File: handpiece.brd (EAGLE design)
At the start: 100 x 82.5 mm, 27 parts, among them IC1 MEGA8-P

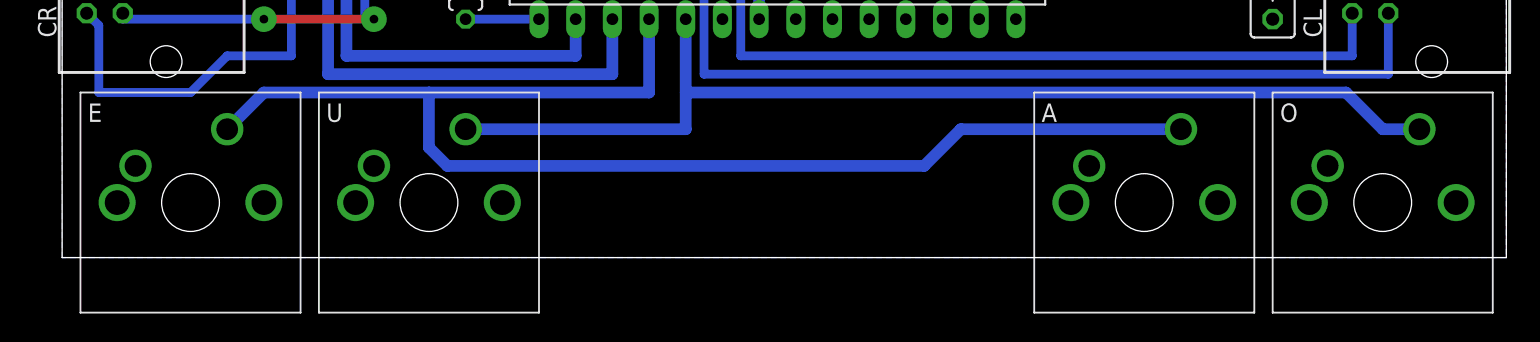
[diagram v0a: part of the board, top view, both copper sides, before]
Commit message: move vocal keys to comply to https://sites.google.com/site/ploverdoc/lesson-1-fingers-and-keys
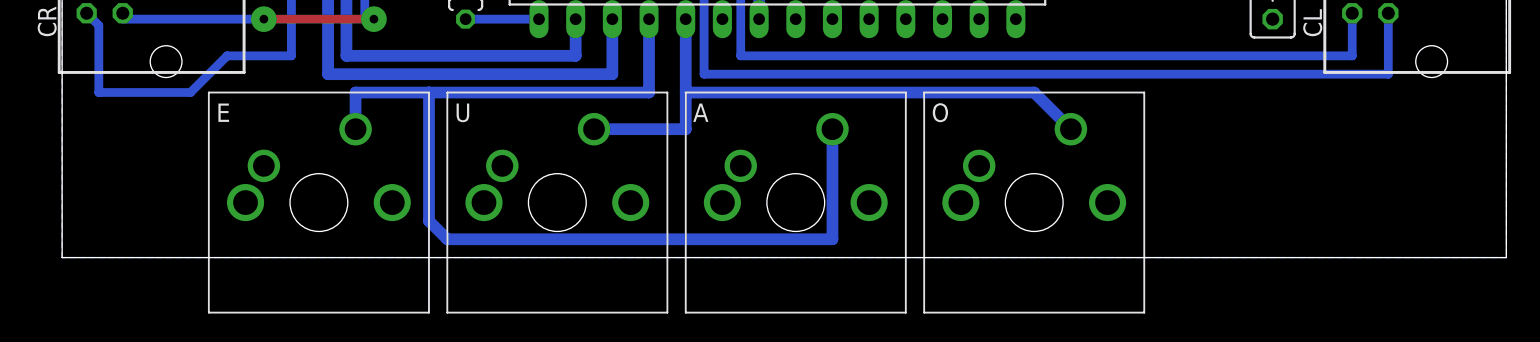
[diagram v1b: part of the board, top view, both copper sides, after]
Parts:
- moved A 24.1 mm to (50.8, 2.54)
- moved O 24.1 mm to (67.3, 2.54)
- moved E 8.89 mm to (17.8, 2.54)
- moved U 8.89 mm to (34.3, 2.54)
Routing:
- net OU: track 74.7 -> 41.7 mm
- net EA: track 92.8 -> 72.9 mm
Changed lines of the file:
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@@
 <?xml version="1.0" encoding="utf-8"?>
 <!DOCTYPE eagle SYSTEM "eagle.dtd">
-<eagle version="6.5.0">
+<eagle version="6.4">
 <drawing>
 <settings>
@@
 <element name="D" library="cherrymx" package="CHERRY-MX-I" value="CHERRY-MX-I" x="91.44" y="52.07"/>
 <element name="Z" library="cherrymx" package="CHERRY-MX-I" value="CHERRY-MX-I" x="91.44" y="35.56"/>
-<element name="E" library="cherrymx" package="CHERRY-MX-I" value="CHERRY-MX-I" x="8.89" y="2.54"/>
-<element name="U" library="cherrymx" package="CHERRY-MX-I" value="CHERRY-MX-I" x="25.4" y="2.54"/>
-<element name="O" library="cherrymx" package="CHERRY-MX-I" value="CHERRY-MX-I" x="91.44" y="2.54"/>
-<element name="A" library="cherrymx" package="CHERRY-MX-I" value="CHERRY-MX-I" x="74.93" y="2.54"/>
+<element name="E" library="cherrymx" package="CHERRY-MX-I" value="CHERRY-MX-I" x="17.78" y="2.54"/>
+<element name="U" library="cherrymx" package="CHERRY-MX-I" value="CHERRY-MX-I" x="34.29" y="2.54"/>
+<element name="O" library="cherrymx" package="CHERRY-MX-I" value="CHERRY-MX-I" x="67.31" y="2.54"/>
+<element name="A" library="cherrymx" package="CHERRY-MX-I" value="CHERRY-MX-I" x="50.8" y="2.54"/>
 <element name="SS0" library="cherrymx" package="CHERRY-MX-I" value="CHERRY-MX-I" x="8.89" y="52.07"/>
 <element name="IC1" library="atmel" package="DIL28-3" value="MEGA8-P" x="49.53" y="19.05">
@@
 <contactref element="CR" pad="2"/>
 <wire x1="50.8" y1="15.24" x2="50.8" y2="22.86" width="0" layer="19" extent="1-1"/>
+<wire x1="46.99" y1="5.08" x2="50.8" y2="15.24" width="0" layer="19" extent="1-1"/>
 <wire x1="71.12" y1="38.1" x2="54.61" y2="38.1" width="0" layer="19" extent="1-1"/>
 </signal>
@@
 <signal name="EA">
 <contactref element="E" pad="PIN-2"/>
-<wire x1="11.43" y1="7.62" x2="13.97" y2="10.16" width="0.8128" layer="16"/>
-<wire x1="13.97" y1="10.16" x2="25.4" y2="10.16" width="0.8128" layer="16"/>
+<wire x1="20.32" y1="7.62" x2="20.32" y2="10.16" width="0.8128" layer="16"/>
+<wire x1="20.32" y1="10.16" x2="25.4" y2="10.16" width="0.8128" layer="16"/>
 <wire x1="25.4" y1="10.16" x2="40.64" y2="10.16" width="0.8128" layer="16"/>
 <contactref element="A" pad="PIN-2"/>
-<wire x1="25.4" y1="10.16" x2="25.4" y2="6.35" width="0.8128" layer="16"/>
-<wire x1="25.4" y1="6.35" x2="26.67" y2="5.08" width="0.8128" layer="16"/>
-<wire x1="26.67" y1="5.08" x2="59.69" y2="5.08" width="0.8128" layer="16"/>
-<wire x1="59.69" y1="5.08" x2="62.23" y2="7.62" width="0.8128" layer="16"/>
-<wire x1="62.23" y1="7.62" x2="77.47" y2="7.62" width="0.8128" layer="16"/>
+<wire x1="25.4" y1="10.16" x2="25.4" y2="1.27" width="0.8128" layer="16"/>
+<wire x1="25.4" y1="1.27" x2="26.67" y2="0" width="0.8128" layer="16"/>
+<wire x1="26.67" y1="0" x2="53.34" y2="0" width="0.8128" layer="16"/>
+<wire x1="53.34" y1="0" x2="53.34" y2="7.62" width="0.8128" layer="16"/>
 <contactref element="IC1" pad="4"/>
 <wire x1="40.64" y1="10.16" x2="40.64" y2="15.24" width="0.8128" layer="16"/>
@@
 <signal name="OU">
 <contactref element="U" pad="PIN-2"/>
-<wire x1="27.94" y1="7.62" x2="43.18" y2="7.62" width="0.8128" layer="16"/>
+<wire x1="36.83" y1="7.62" x2="43.18" y2="7.62" width="0.8128" layer="16"/>
 <contactref element="O" pad="PIN-2"/>
 <wire x1="43.18" y1="7.62" x2="43.18" y2="10.16" width="0.8128" layer="16"/>
-<wire x1="43.18" y1="10.16" x2="88.9" y2="10.16" width="0.8128" layer="16"/>
-<wire x1="88.9" y1="10.16" x2="91.44" y2="7.62" width="0.8128" layer="16"/>
-<wire x1="91.44" y1="7.62" x2="93.98" y2="7.62" width="0.8128" layer="16"/>
+<wire x1="43.18" y1="10.16" x2="67.31" y2="10.16" width="0.8128" layer="16"/>
+<wire x1="67.31" y1="10.16" x2="69.85" y2="7.62" width="0.8128" layer="16"/>
 <contactref element="IC1" pad="5"/>
 <wire x1="43.18" y1="15.24" x2="43.18" y2="10.16" width="0.8128" layer="16"/>

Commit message: exchange minidin connectors with raw soldering pads and strain-releive holes
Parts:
- removed CL, CR: (no value), con-yamaichi:MDIN06SS
- added JPL, JPR: (no value), pinhead:1X04
- moved C1 7.62 mm to (83.8, 11.4)
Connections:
- net GND: now also JPL.1, JPR.1; no longer CL.1, CL.2, CR.1, CR.2
- net SCL: now also JPL.4, JPR.4; no longer CL.6, CR.6
- net SDA: now also JPL.3, JPR.3; no longer CL.4, CR.4
- net VCC: now also JPL.2, JPR.2; no longer CL.3, CL.5, CR.3, CR.5
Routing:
- net SCL: track 130.1 -> 113.4 mm
- net VCC: track 108.5 -> 124.5 mm
- net SDA: track 130.1 -> 138.2 mm
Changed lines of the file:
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@@
 <layer number="43" name="vRestrict" color="2" fill="10" visible="yes" active="yes"/>
 <layer number="44" name="Drills" color="7" fill="1" visible="no" active="yes"/>
-<layer number="45" name="Holes" color="7" fill="1" visible="no" active="yes"/>
+<layer number="45" name="Holes" color="7" fill="1" visible="yes" active="yes"/>
 <layer number="46" name="Milling" color="3" fill="1" visible="no" active="yes"/>
 <layer number="47" name="Measures" color="7" fill="1" visible="no" active="yes"/>
@@
 <wire x1="100" y1="81.27" x2="0" y2="81.27" width="0" layer="20"/>
 <wire x1="0" y1="81.27" x2="0" y2="-1.27" width="0" layer="20"/>
+<hole x="3.81" y="16.51" drill="2.2"/>
+<hole x="3.81" y="10.16" drill="2.2"/>
+<hole x="95.25" y="16.51" drill="2.2"/>
+<hole x="95.25" y="10.16" drill="2.2"/>
 </plain>
 <attributes>
@@
 </element>
 <element name="R1" library="rcl" package="0207/7" value="10k" x="27.94" y="19.05" rot="R90"/>
-<element name="C1" library="rcl" package="C075-032X103" value="100n" x="83.82" y="19.05" rot="R270"/>
-<element name="CL" library="con-yamaichi" package="MDIN06SS" value="" x="100.33" y="19.05" rot="R90">
-<attribute name="OC_NEWARK" value="unknown" x="100.33" y="19.05" size="1.778" layer="27" rot="R90" display="off"/>
-<attribute name="MPN" value="" x="100.33" y="19.05" size="1.778" layer="27" rot="R90" display="off"/>
-<attribute name="MF" value="" x="100.33" y="19.05" size="1.778" layer="27" rot="R90" display="off"/>
-<attribute name="OC_FARNELL" value="unknown" x="100.33" y="19.05" size="1.778" layer="27" rot="R90" display="off"/>
-</element>
-<element name="CR" library="con-yamaichi" package="MDIN06SS" value="" x="12.7" y="19.05" rot="R90">
-<attribute name="OC_NEWARK" value="unknown" x="12.7" y="19.05" size="1.778" layer="27" rot="R90" display="off"/>
-<attribute name="MPN" value="" x="12.7" y="19.05" size="1.778" layer="27" rot="R90" display="off"/>
-<attribute name="MF" value="" x="12.7" y="19.05" size="1.778" layer="27" rot="R90" display="off"/>
-<attribute name="OC_FARNELL" value="unknown" x="12.7" y="19.05" size="1.778" layer="27" rot="R90" display="off"/>
-</element>
+<element name="C1" library="rcl" package="C075-032X103" value="100n" x="83.82" y="11.43" rot="R270"/>
+<element name="JPL" library="pinhead" package="1X04" value="" x="7.62" y="22.86"/>
+<element name="JPR" library="pinhead" package="1X04" value="" x="91.44" y="22.86" rot="R180"/>
 </elements>
 <signals>
@@
 <contactref element="D" pad="PIN-1"/>
 <contactref element="Z" pad="PIN-1"/>
-<contactref element="CL" pad="1"/>
-<contactref element="CL" pad="2"/>
 <contactref element="E" pad="PIN-1"/>
 <contactref element="U" pad="PIN-1"/>
@@
 <vertex x="0" y="-1.27"/>
 </polygon>
-<contactref element="CR" pad="1"/>
-<contactref element="CR" pad="2"/>
-<wire x1="50.8" y1="15.24" x2="50.8" y2="22.86" width="0" layer="19" extent="1-1"/>
+<contactref element="JPL" pad="1"/>
+<contactref element="JPR" pad="1"/>
+<wire x1="50.8" y1="22.86" x2="50.8" y2="15.24" width="0" layer="19" extent="1-1"/>
 <wire x1="46.99" y1="5.08" x2="50.8" y2="15.24" width="0" layer="19" extent="1-1"/>
 <wire x1="71.12" y1="38.1" x2="54.61" y2="38.1" width="0" layer="19" extent="1-1"/>
@@
 <contactref element="R1" pad="2"/>
 <contactref element="C1" pad="1"/>
-<contactref element="CL" pad="3"/>
-<contactref element="CL" pad="5"/>
 <wire x1="27.94" y1="22.86" x2="27.94" y2="20.32" width="0.8128" layer="16"/>
 <wire x1="27.94" y1="20.32" x2="48.26" y2="20.32" width="0.8128" layer="16"/>
@@
 <wire x1="53.34" y1="22.86" x2="53.34" y2="20.32" width="0.8128" layer="16"/>
 <wire x1="53.34" y1="17.78" x2="83.82" y2="17.78" width="0.8128" layer="16"/>
-<wire x1="83.82" y1="17.78" x2="83.82" y2="22.86" width="0.8128" layer="16"/>
-<wire x1="83.82" y1="22.86" x2="88.92" y2="22.86" width="0.8128" layer="16"/>
-<wire x1="91.83" y1="22.45" x2="89.33" y2="22.45" width="0.8128" layer="16"/>
-<wire x1="89.33" y1="22.45" x2="88.92" y2="22.86" width="0.8128" layer="16"/>
-<contactref element="CR" pad="3"/>
-<contactref element="CR" pad="5"/>
-<wire x1="1.7" y1="22.45" x2="4.2" y2="22.45" width="0.8128" layer="16"/>
-<wire x1="4.2" y1="22.45" x2="13.97" y2="22.45" width="0.8128" layer="16"/>
-<wire x1="13.97" y1="22.45" x2="13.97" y2="22.86" width="0.8128" layer="16"/>
-<via x="13.97" y="22.86" extent="1-16" drill="0.6" diameter="1.778" shape="square"/>
-<wire x1="13.97" y1="22.86" x2="25.4" y2="22.86" width="0.8128" layer="1"/>
+<wire x1="83.82" y1="17.78" x2="83.82" y2="15.24" width="0.8128" layer="16"/>
+<via x="15.24" y="22.86" extent="1-16" drill="0.6" diameter="1.778" shape="square"/>
+<wire x1="15.24" y1="22.86" x2="25.4" y2="22.86" width="0.8128" layer="1"/>
 <via x="25.4" y="22.86" extent="1-16" drill="0.6" diameter="1.778" shape="square"/>
 <wire x1="53.34" y1="17.78" x2="53.34" y2="20.32" width="0.8128" layer="16"/>
 <wire x1="53.34" y1="20.32" x2="48.26" y2="20.32" width="0.8128" layer="16"/>
 <wire x1="25.4" y1="22.86" x2="27.94" y2="22.86" width="0.8128" layer="16"/>
+<contactref element="JPL" pad="2"/>
+<contactref element="JPR" pad="2"/>
+<wire x1="15.24" y1="22.86" x2="15.24" y2="25.4" width="0.6096" layer="16"/>
+<wire x1="15.24" y1="25.4" x2="6.35" y2="25.4" width="0.6096" layer="16"/>
+<wire x1="6.35" y1="25.4" x2="6.35" y2="22.86" width="0.6096" layer="16"/>
+<wire x1="83.82" y1="15.24" x2="83.82" y2="27.94" width="0.8128" layer="16"/>
+<wire x1="83.82" y1="27.94" x2="92.71" y2="27.94" width="0.8128" layer="16"/>
+<wire x1="92.71" y1="27.94" x2="92.71" y2="22.86" width="0.8128" layer="16"/>
 </signal>
 <signal name="N$2">
@@
 <signal name="SCL">
 <contactref element="IC1" pad="28"/>
-<contactref element="CL" pad="6"/>
-<contactref element="CR" pad="6"/>
-<wire x1="89.33" y1="15.65" x2="89.33" y2="12.7" width="0.6096" layer="16"/>
-<wire x1="89.33" y1="12.7" x2="46.99" y2="12.7" width="0.6096" layer="16"/>
+<wire x1="87.63" y1="12.7" x2="46.99" y2="12.7" width="0.6096" layer="16"/>
 <wire x1="46.99" y1="12.7" x2="46.99" y2="19.05" width="0.6096" layer="16"/>
 <wire x1="46.99" y1="19.05" x2="23.495" y2="19.05" width="0.6096" layer="16"/>
@@
 <wire x1="27.94" y1="25.4" x2="30.48" y2="22.86" width="0.6096" layer="16"/>
 <wire x1="30.48" y1="22.86" x2="33.02" y2="22.86" width="0.6096" layer="16"/>
-<wire x1="23.495" y1="19.05" x2="13.97" y2="19.05" width="0.6096" layer="1"/>
-<wire x1="13.97" y1="19.05" x2="15.875" y2="19.05" width="0.6096" layer="16"/>
-<wire x1="15.875" y1="19.05" x2="15.875" y2="12.7" width="0.6096" layer="16"/>
-<wire x1="15.875" y1="12.7" x2="11.43" y2="12.7" width="0.6096" layer="16"/>
-<wire x1="11.43" y1="12.7" x2="8.89" y2="10.16" width="0.6096" layer="16"/>
-<wire x1="8.89" y1="10.16" x2="2.54" y2="10.16" width="0.6096" layer="16"/>
-<wire x1="2.54" y1="10.16" x2="2.54" y2="14.81" width="0.6096" layer="16"/>
-<wire x1="2.54" y1="14.81" x2="1.7" y2="15.65" width="0.6096" layer="16"/>
-<via x="13.97" y="19.05" extent="1-16" drill="0.6" diameter="1.778" shape="square"/>
+<wire x1="23.495" y1="19.05" x2="15.24" y2="19.05" width="0.6096" layer="1"/>
+<via x="15.24" y="19.05" extent="1-16" drill="0.6" diameter="1.778" shape="square"/>
 <via x="23.495" y="19.05" extent="1-16" drill="0.6" diameter="1.778" shape="square"/>
+<contactref element="JPL" pad="4"/>
+<contactref element="JPR" pad="4"/>
+<wire x1="15.24" y1="19.05" x2="11.43" y2="19.05" width="0.6096" layer="16"/>
+<wire x1="11.43" y1="19.05" x2="11.43" y2="22.86" width="0.6096" layer="16"/>
+<wire x1="87.63" y1="12.7" x2="87.63" y2="22.86" width="0.6096" layer="16"/>
 </signal>
 <signal name="SDA">
 <contactref element="IC1" pad="27"/>
-<contactref element="CL" pad="4"/>
-<contactref element="CR" pad="4"/>
-<wire x1="91.83" y1="15.65" x2="91.83" y2="11.43" width="0.6096" layer="16"/>
-<wire x1="91.83" y1="11.43" x2="44.45" y2="11.43" width="0.6096" layer="16"/>
+<wire x1="90.17" y1="11.43" x2="44.45" y2="11.43" width="0.6096" layer="16"/>
 <wire x1="44.45" y1="11.43" x2="44.45" y2="17.145" width="0.6096" layer="16"/>
 <wire x1="44.45" y1="17.145" x2="20.955" y2="17.145" width="0.6096" layer="16"/>
@@
 <wire x1="20.955" y1="17.145" x2="20.955" y2="15.24" width="0.6096" layer="16"/>
 <wire x1="20.955" y1="15.24" x2="21.59" y2="15.24" width="0.6096" layer="16"/>
-<wire x1="21.59" y1="15.24" x2="13.97" y2="15.24" width="0.6096" layer="1"/>
-<wire x1="13.97" y1="15.24" x2="4.2" y2="15.24" width="0.6096" layer="16"/>
-<wire x1="4.2" y1="15.24" x2="4.2" y2="15.65" width="0.6096" layer="16"/>
-<via x="13.97" y="15.24" extent="1-16" drill="0.6" diameter="1.778" shape="square"/>
+<wire x1="21.59" y1="15.24" x2="15.24" y2="15.24" width="0.6096" layer="1"/>
+<via x="15.24" y="15.24" extent="1-16" drill="0.6" diameter="1.778" shape="square"/>
 <via x="21.59" y="15.24" extent="1-16" drill="0.6" diameter="1.778" shape="square"/>
+<contactref element="JPL" pad="3"/>
+<contactref element="JPR" pad="3"/>
+<wire x1="15.24" y1="15.24" x2="8.89" y2="15.24" width="0.6096" layer="16"/>
+<wire x1="8.89" y1="15.24" x2="8.89" y2="22.86" width="0.6096" layer="16"/>
+<wire x1="90.17" y1="11.43" x2="90.17" y2="22.86" width="0.6096" layer="16"/>
 </signal>
 </signals>
